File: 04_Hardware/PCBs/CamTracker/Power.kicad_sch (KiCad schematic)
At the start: 90 parts, among them J2 67996-100HLF, U1 SC206EEMDA-G51-UGNDA, U2 AP64502QSP-13, U3 AP7335-WG-7, U4 AP61100Z6-7, U5 AP61100Z6-7, U6 AP7179DSKZ20-13

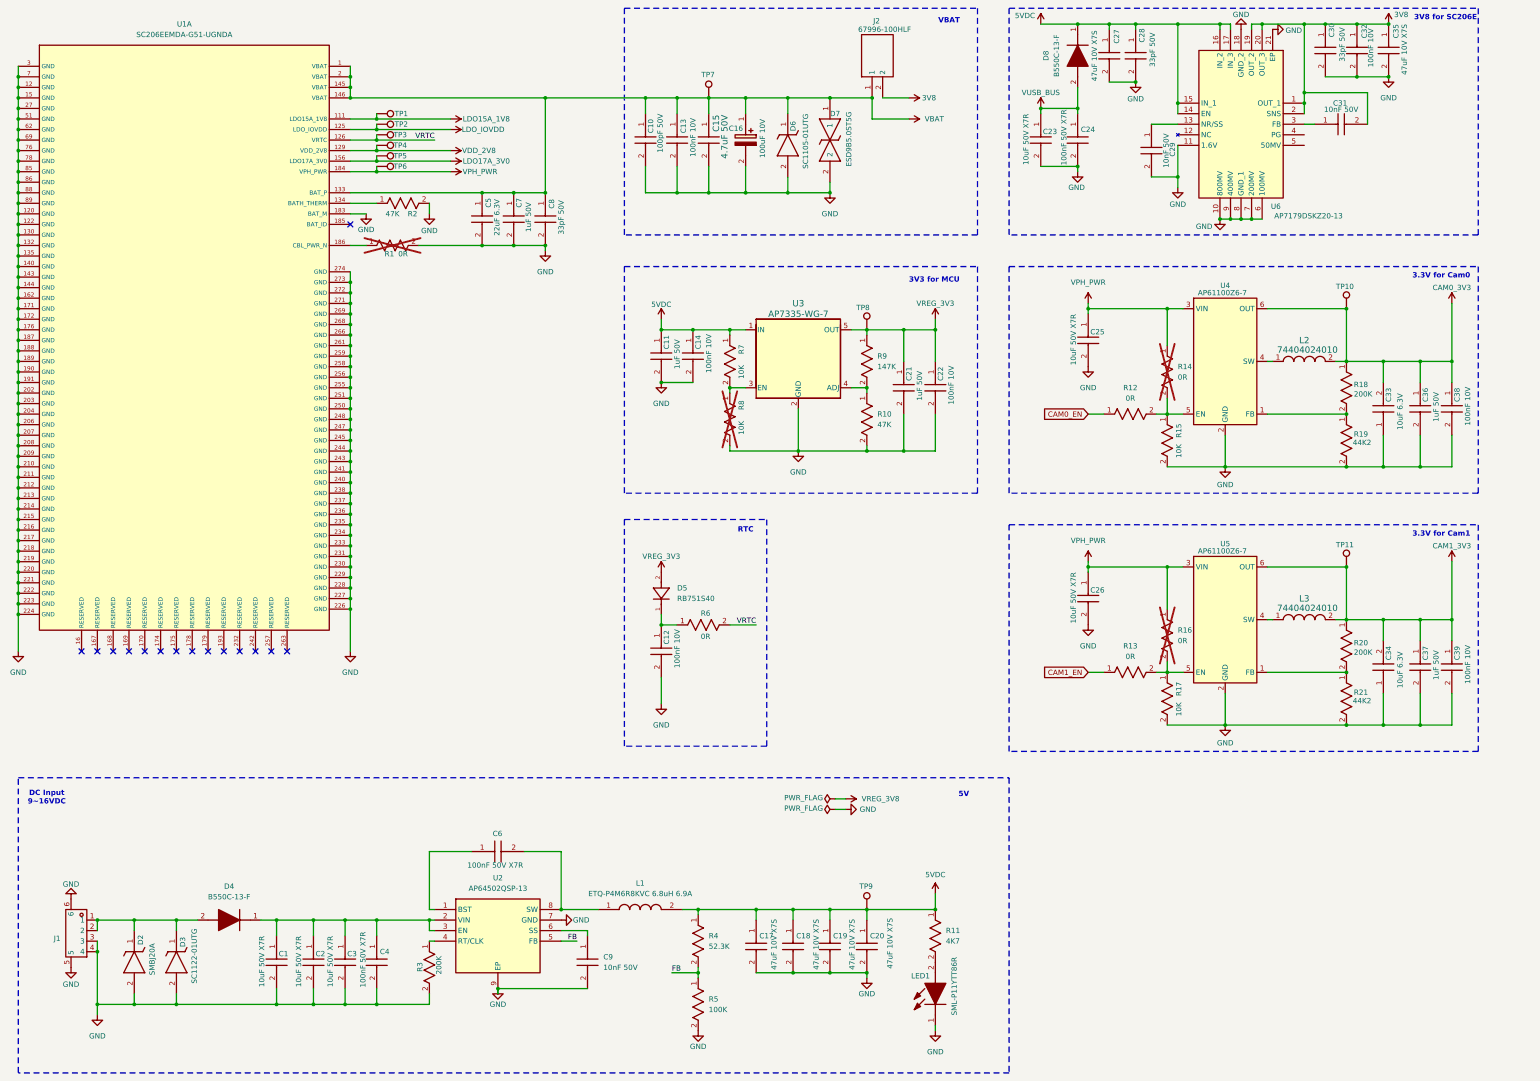
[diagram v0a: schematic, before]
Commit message: feat: Completed Placement v1 in Layout
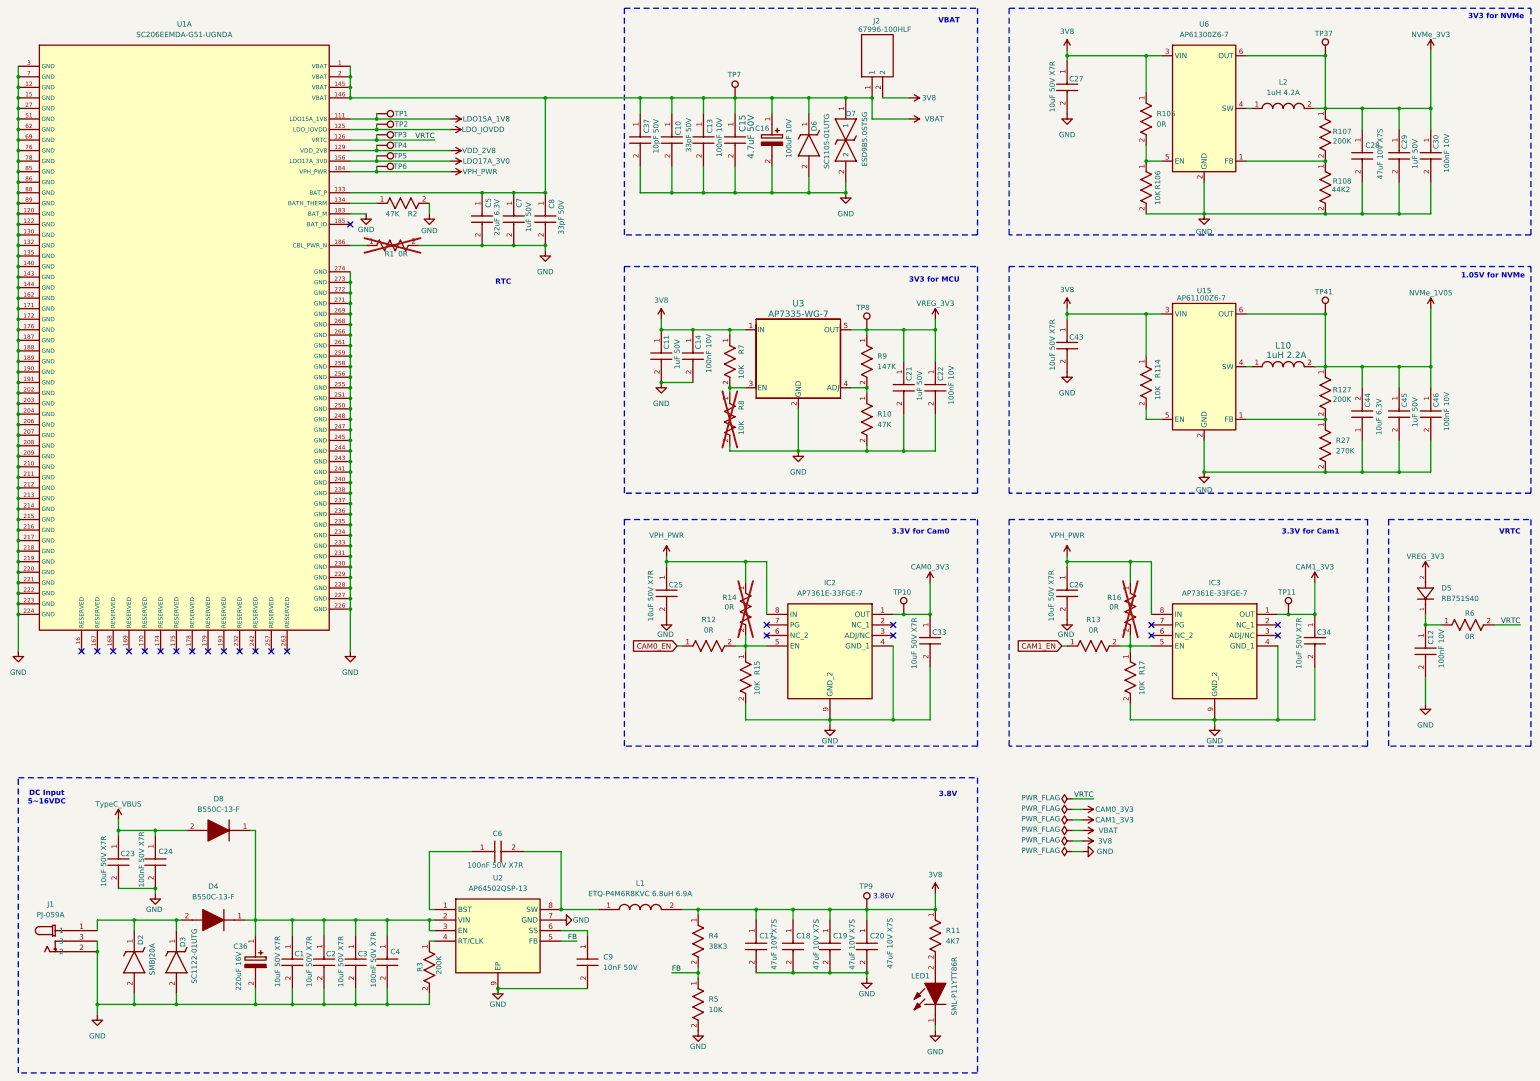
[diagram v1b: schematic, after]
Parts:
- removed C10: 100pF 50V, 000MCLib:CAPC1005X55N, symbol 000MCLib:GRM1555C1H101JA01J
- removed C27, C35: 47uF 10V X7S, 000MCLib:CAPC3225X280N, symbol 000MCLib:CGA6P1X7S1A476M250AC
- removed C28, C30: 33pF 50V, 000MCLib:CAPC1005X55N, symbol 000MCLib:GRM1555C1H330JA01D
- removed C29, C31: 10nF 50V, 000MCLib:CAPC1005X55N, symbol 000MCLib:GRM155R71H103KA88D
- removed C32, C38, C39: 100nF 10V, 000MCLib:CAPC1005X55N, symbol 000MCLib:GRM155R71A104KA01D
- removed C33, C34: 10uF 6.3V, 000MCLib:CAPC1005X55N, symbol 000MCLib:GRM155R60J106ME15D
- removed C36, C37: 1uF 50V, 000MCLib:CAPC1005X55N, symbol 000MCLib:GRM155R61H105KE05D
- removed J1: ~, 000MCLib:CONN-SMD_1.25-4PLT, symbol 000MCLib:1.25-4P LT
- removed L2, L3: 74404024010, 000MCLib:IND_WE-LQS_2512_WRE, symbol 000MCLib:74404024010
- removed R18, R20: 200K, 000MCLib:RC0402N_YAG, symbol 000MCLib:RC0402FR-07200KL
- removed R19, R21: 44K2, 000MCLib:RC0402N_YAG, symbol 000MCLib:RC0402FR-0744K2L
- removed R4: 52.3K, 000MCLib:RC0402N_YAG, symbol 000MCLib:RT0402BRD0752K3L
- removed R5: 100K, 000MCLib:RC0402N_YAG, symbol 000MCLib:RC0402JR-07100KL
- removed U4, U5: AP61100Z6-7, 000MCLib:SOT50P162X60-6N, symbol 000MCLib:AP61100Z6-7
- removed U6: AP7179DSKZ20-13, 000MCLib:QFN50P350X350X80-21N-D, symbol 000MCLib:AP7179DSKZ20-13
- added C10: 33pF 50V, 000MCLib:CAPC1005X55N, symbol 000MCLib:GRM1555C1H330JA01D
- added C27, C33, C34, C43: 10uF 50V X7R, 000MCLib:CAPC3216X190N, symbol 000MCLib:CL31B106KBK6PJE
- added C28: 47uF 10V X7S, 000MCLib:CAPC3225X280N, symbol 000MCLib:CGA6P1X7S1A476M250AC
- added C29, C45: 1uF 50V, 000MCLib:CAPC1005X55N, symbol 000MCLib:GRM155R61H105KE05D
- added C30, C46: 100nF 10V, 000MCLib:CAPC1005X55N, symbol 000MCLib:GRM155R71A104KA01D
- added C36: 220uF 16V, 000MCLib:CAPAE830X1000N, symbol 000MCLib:A765KN227M1CLAE016
- added C37: 10pF 50V, 000MCLib:CAPC1005X55N, symbol 000MCLib:GRM1555C1H100JA01D
- added C44: 10uF 6.3V, 000MCLib:CAPC1005X55N, symbol 000MCLib:GRM155R60J106ME15D
- added IC2, IC3: AP7361E-33FGE-7, 000MCLib:SON65P300X300X63-9N, symbol 000MCLib:AP7361E-33FGE-7
- added J1: PJ-059A, 000MCLib:PJ059A, symbol 000MCLib:PJ-059A
- added L10: 1uH 2.2A, 000MCLib:IND_WE-LQS_2512_WRE, symbol 000MCLib:74404024010
- added L2: 1uH 4.2A, 000MCLib:LSEUC3225HKT1R0M, symbol 000MCLib:LSEUC3225HKT1R0M
- added R105: 0R, 000MCLib:RESC2012X50N, symbol 000MCLib:CRCW08050000Z0EA
- added R106, R114, R5: 10K, 000MCLib:RC0402N_YAG, symbol 000MCLib:RC0402JR-0710KL
- added R107, R127: 200K, 000MCLib:RC0402N_YAG, symbol 000MCLib:RC0402FR-07200KL
- added R108: 44K2, 000MCLib:RC0402N_YAG, symbol 000MCLib:RC0402FR-0744K2L
- added R27: 270K, 000MCLib:RC0402N_YAG, symbol 000MCLib:RC0402FR-07270KL
- added R4: 38K3, 000MCLib:RC0402N_YAG, symbol 000MCLib:AF0402FR-0738K3L
- added TP37, TP41: TestPoint, TestPoint:TestPoint_Pad_D1.0mm, symbol 000MCLib:TestPoint
- added U15: AP61100Z6-7, 000MCLib:SOT50P162X60-6N, symbol 000MCLib:AP61100Z6-7
- added U6: AP61300Z6-7, 000MCLib:SOT50P162X60-6N, symbol 000MCLib:AP61300Z6-7
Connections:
- net 3V8: now also C11.1, C14.1, C17.1, C18.1, C19.1, C20.1, L1.2, R11.1, R7.1, TP9.1, U3.1 (IN), C27.1, C43.1, R105.1, R114.1, R4.1, U15.3 (VIN), U6.3 (VIN)
- net CAM0_3V3: now also C33.1, IC2.1 (OUT)
- net CAM1_3V3: now also C34.1, IC3.1 (OUT)
- net FB: now also R4.2, R5.1
- net GND: now also C10.2, C27.2, C28.2, C29.2, C30.2, C33.2, C34.2, C36.2 (-), C37.2, C43.2, C44.1, C45.2, C46.2, IC2.4 (GND_1), IC2.9 (GND_2), IC3.4 (GND_1), IC3.9 (GND_2), J1.2, J1.3, R106.2, R108.2, R27.2, R5.2, U15.2 (GND), U6.2 (GND)
- net VBAT: now also C10.1, C37.1
- net VPH_PWR: now also IC2.8 (IN), IC3.8 (IN)
- net at D2.1 (K), D3.1 (K), D4.2 (A): now also J1.1
- net at C1.1, C2.1, C3.1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: now also D8.1 (K), C36.1 (+)
- net at R12.2, R14.2, R15.1: now also IC2.5 (EN)
- net at R13.2, R16.2, R17.1: now also IC3.5 (EN)
- removed net 5VDC: C11.1, C14.1, C17.1, C18.1, C19.1, C20.1, D8.1 (K), L1.2, R11.1, R7.1, TP9.1, U3.1 (IN)
- net VUSB_BUS renamed TypeC_VBUS
- new net: R107.2, R108.1, U6.1 (FB)
- new net: R127.2, R27.1, U15.1 (FB)
- new net: L2.1, U6.4 (SW)
- new net: R105.2, R106.1, U6.5 (EN)
- new net: R114.2, U15.5 (EN)
- new net: L10.1, U15.4 (SW)
- new net NVMe_1V05: C44.2, C45.1, C46.1, L10.2, R127.1, TP41.1, U15.6 (OUT)
- new net NVMe_3V3: C28.1, C29.1, C30.1, L2.2, R107.1, TP37.1, U6.6 (OUT)
- no-connect marks 15 -> 23
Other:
- note added: "1.05V for NVMe"
- note added: "3.86V"
- note added: "3.8V"
- note added: "3V3 for NVMe"
- note added: "DC Input 5~16VDC"
- note added: "VRTC"
- note removed: "3V8 for SC206E"
- note removed: "5V"
- note removed: "DC Input 9~16VDC"
- moved on the sheet: C1, C12, C13, C15, C16, C2, C23, C24, C3, C4, D4, D5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

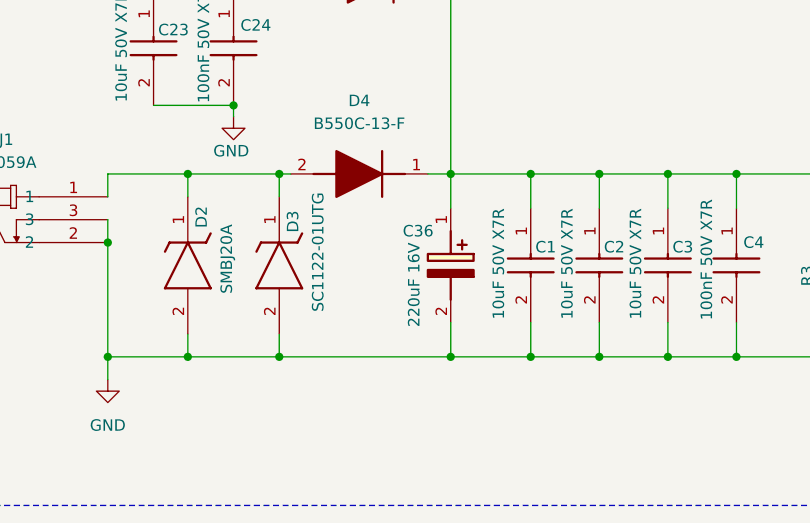
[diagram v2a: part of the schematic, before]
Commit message: feat(PCB): DC input Capacitor has been changed
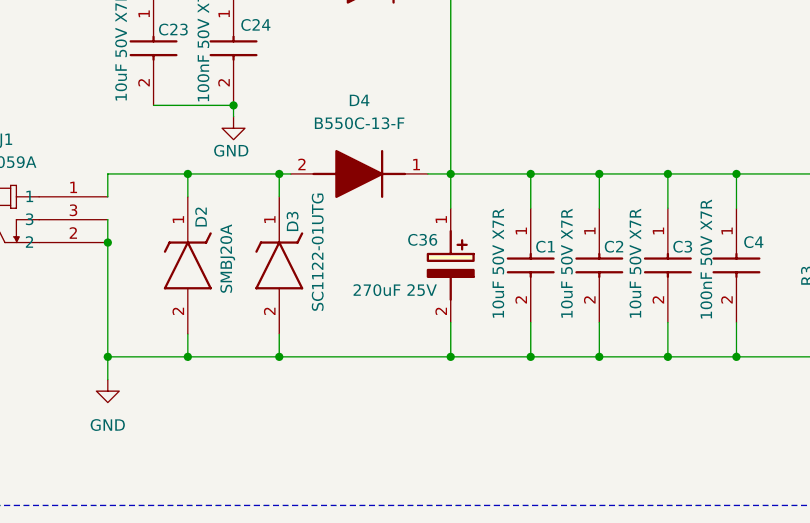
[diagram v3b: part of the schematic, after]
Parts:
- removed C36: 220uF 16V, 000MCLib:CAPAE830X1000N, symbol 000MCLib:A765KN227M1CLAE016
- added C36: 270uF 25V, 000MCLib:16SVPT560M, symbol 000MCLib:25SVPG270M
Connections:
- net GND: now also C36.2 (-)
- net at C1.1, C2.1, C3.1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: now also C36.1 (+)
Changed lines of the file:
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@@
 	)
 	(symbol
+		(lib_id "000MCLib:25SVPG270M")
+		(at 83.82 240.03 270)
+		(unit 1)
+		(exclude_from_sim no)
+		(in_bom yes)
+		(on_board yes)
+		(dnp no)
+		(property "Reference" "C36"
+			(at 78.994 243.586 90)
+			(effects
+				(font
+					(size 1.27 1.27)
+				)
+				(justify left)
+			)
+		)
+		(property "Value" "270uF 25V"
+			(at 72.898 249.174 90)
+			(effects
+				(font
+					(size 1.27 1.27)
+				)
+				(justify left)
+			)
+		)
+		(property "Footprint" "000MCLib:16SVPT560M"
+			(at -12.37 248.92 0)
+			(effects
+				(font
+					(size 1.27 1.27)
+				)
+				(justify left top)
+				(hide yes)
+			)
+		)
+		(property "Datasheet" "https://industrial.panasonic.com/cdbs/www-data/pdf/AAB8000/AAB8000C175.pdf"
+			(at -112.37 248.92 0)
+			(effects
+				(font
+					(size 1.27 1.27)
+				)
+				(justify left top)
+				(hide yes)
+			)
+		)
+		(property "Description" "Capacitor 270uF 25V Electrolitic Low ESR High ripple current 105  5000 h"
+			(at 83.82 240.03 0)
+			(effects
+				(font
+					(size 1.27 1.27)
+				)
+				(hide yes)
+			)
+		)
+		(property "Manufacturer" "Panasonic"
+			(at -612.37 248.92 0)
+			(effects
+				(font
+					(size 1.27 1.27)
+				)
+				(justify left top)
+				(hide yes)
+			)
+		)
+		(property "Part Number" "25SVPG270M"
+			(at -712.37 248.92 0)
+			(effects
+				(font
+					(size 1.27 1.27)
+				)
+				(justify left top)
+				(hide yes)
+			)
+		)
+		(pin "1"
+		)
+		(pin "2"
+		)
+		(instances
+			(project "CamTracker"
+				(path "/38605b01-fdd9-41de-8a8b-501279ee3e8a/04241d8f-a156-493c-8d6a-b2fd4005e365"
+					(reference "C36")
+					(unit 1)
+				)
+			)
+		)
+	)
+	(symbol
 		(lib_id "000MCLib:CL31B106KBK6PJE")
 		(at 279.4 151.13 270)
@@
 					(unit 1)
 				)
-			)
-		)
-	)
-	(symbol
-		(lib_id "000MCLib:A765KN227M1CLAE016")
-		(at 83.82 240.03 270)
-		(unit 1)
-		(exclude_from_sim no)
-		(in_bom yes)
-		(on_board yes)
-		(dnp no)
-		(property "Reference" "C36"
-			(at 78.486 242.57 90)
-			(effects
-				(font
-					(size 1.27 1.27)
-				)
-				(justify left)
-			)
-		)
-		(property "Value" "220uF 16V"
-			(at 79.756 243.84 0)
-			(effects
-				(font
-					(size 1.27 1.27)
-				)
-				(justify left)
-			)
-		)
-		(property "Footprint" "000MCLib:CAPAE830X1000N"
-			(at -12.37 248.92 0)
-			(effects
-				(font
-					(size 1.27 1.27)
-				)
-				(justify left top)
-				(hide yes)
-			)
-		)
-		(property "Datasheet" "https://content.kemet.com/datasheets/KEM_A4070_A765.pdf"
-			(at -112.37 248.92 0)
-			(effects
-				(font
-					(size 1.27 1.27)
-				)
-				(justify left top)
-				(hide yes)
-			)
-		)
-		(property "Description" "Capacitor 220 uF 16 VDC 16 mOhms, Polymer Aluminum"
-			(at 83.82 240.03 0)
-			(effects
-				(font
-					(size 1.27 1.27)
-				)
-				(hide yes)
-			)
-		)
-		(property "Manufacturer" "KEMET"
-			(at -612.37 248.92 0)
-			(effects
-				(font
-					(size 1.27 1.27)
-				)
-				(justify left top)
-				(hide yes)
-			)
-		)
-		(property "Part Number" "A765KN227M1CLAE016"
-			(at -712.37 248.92 0)
-			(effects
-				(font
-					(size 1.27 1.27)
-				)
-				(justify left top)
-				(hide yes)
-			)
-		)
-		(property "Manufacturer Name" ""
-			(at 83.82 240.03 90)
-			(effects
-				(font
-					(size 1.27 1.27)
-				)
-				(hide yes)
-			)
-		)
-		(property "Part_Number" ""
-			(at 83.82 240.03 90)
-			(effects
-				(font
-					(size 1.27 1.27)
-				)
-				(hide yes)
-			)
-		)
-		(property "Part Name" ""
-			(at 83.82 240.03 90)
-			(effects
-				(font
-					(size 1.27 1.27)
-				)
-				(hide yes)
-			)
-		)
-		(pin "2"
-		)
-		(pin "1"
-		)
-		(instances
-			(project ""
-				(path "/38605b01-fdd9-41de-8a8b-501279ee3e8a/04241d8f-a156-493c-8d6a-b2fd4005e365"
-					(reference "C36")
-					(unit 1)
-				)

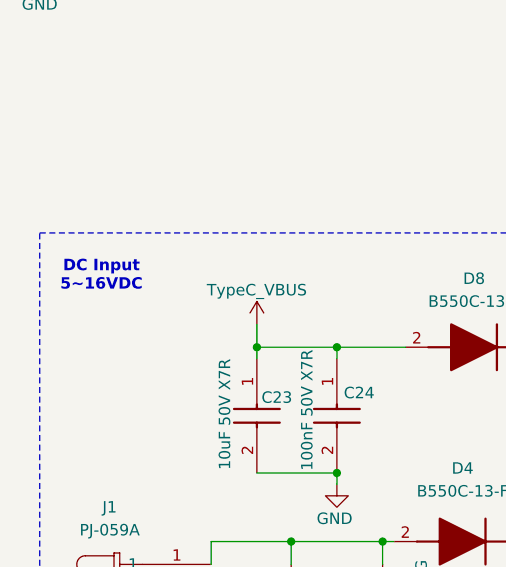
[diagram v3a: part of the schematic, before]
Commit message: feat(PCB): Added GPIO IN to SC206E from the MCU
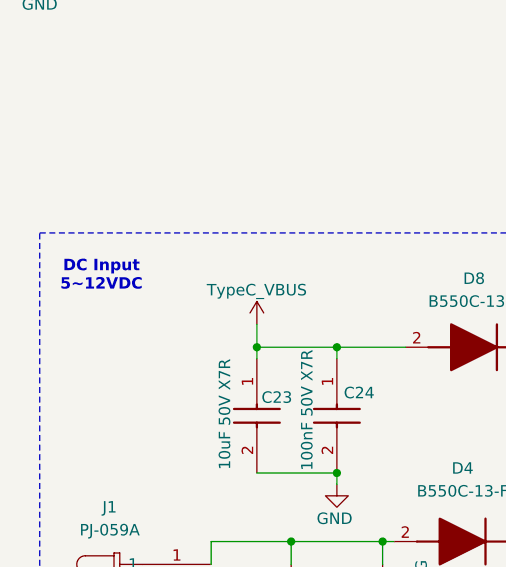
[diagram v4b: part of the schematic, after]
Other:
- note added: "DC Input 5~12VDC"
- note removed: "DC Input 5~16VDC"
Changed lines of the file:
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@@
 		)
 	)
-	(text "DC Input\n5~16VDC"
+	(text "DC Input\n5~12VDC"
 		(exclude_from_sim no)
 		(at 33.528 206.756 0)

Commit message: feat(PCB): finalize PCB design and generate BOM/Gerbers
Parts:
- R105, R12, R13, R14, R16, R6: Height 0.5 -> (none); Mouser Part Number 71-CRCW0805-0-E3 -> (none); Mouser Price/Stock https://www.mouser.co.uk/ProductDetail/Vishay-Dale/CRCW0805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 -> (none)
